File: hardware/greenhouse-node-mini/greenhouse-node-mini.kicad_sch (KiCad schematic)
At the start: 43 parts, among them J1 Molex_KK_396_1x2, J2 JST_XH_2.54mm_1x2, J3 Conn_01x05_Female, J4 Molex_KK_396_1x2, J5 JST_XH_2.54mm_1x4, SW1 SW_Push, U1 ATtiny84A-P, U2 L7805, U3 PCF8574, U4 L298HN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

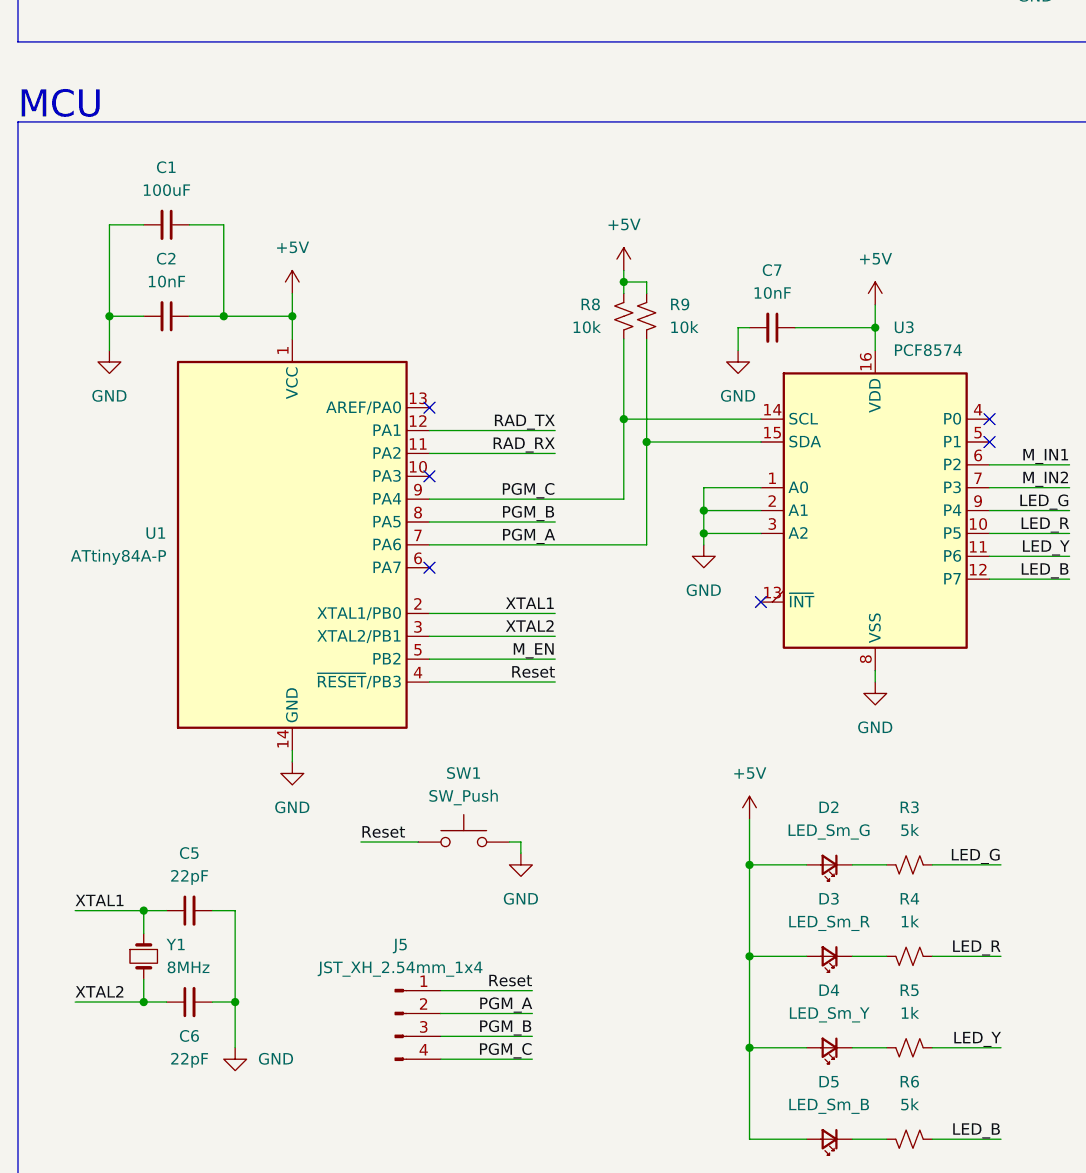
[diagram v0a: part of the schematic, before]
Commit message: Add TODO's for caps
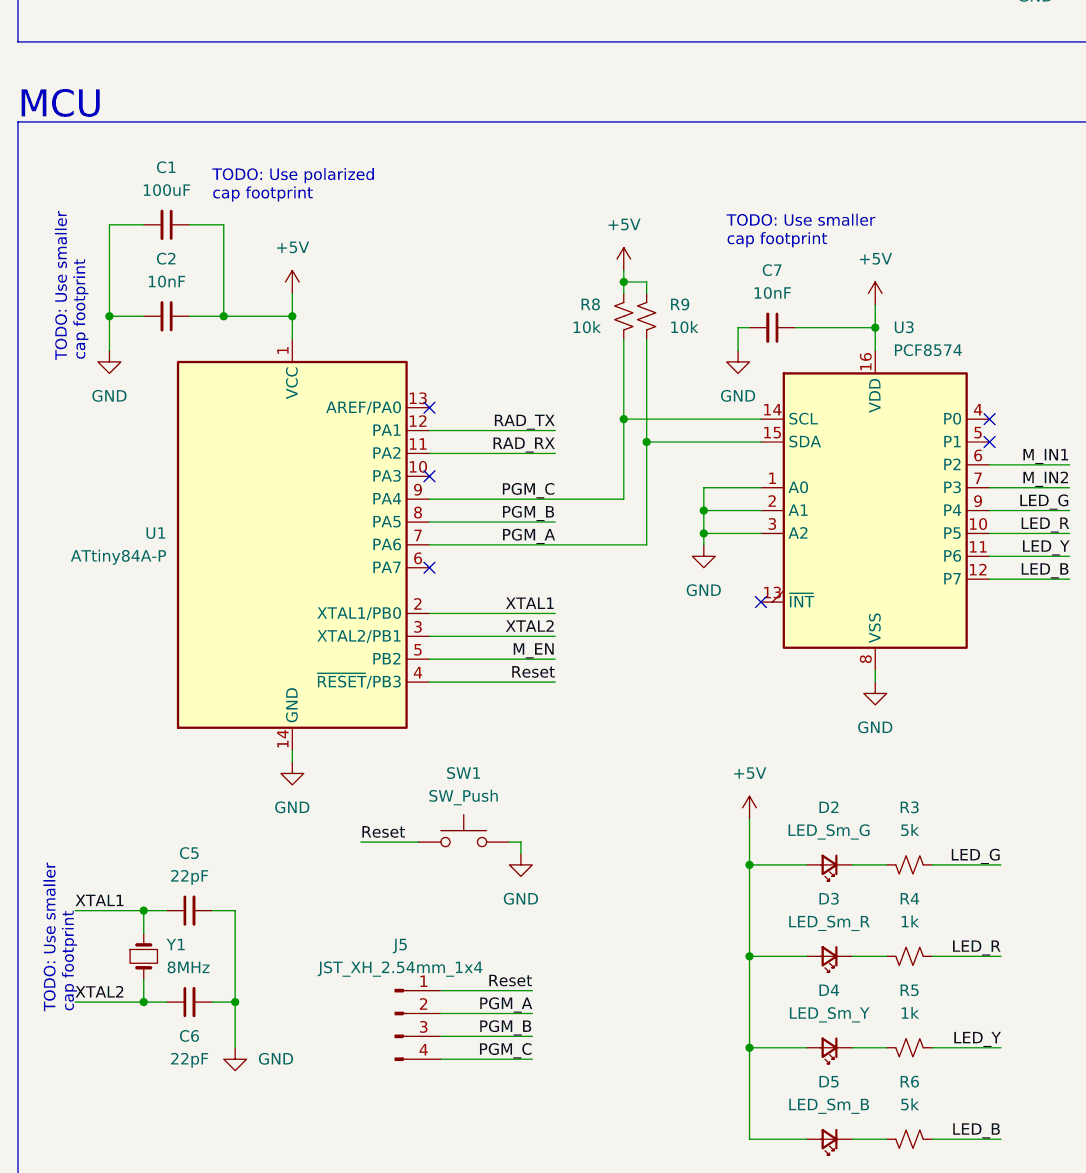
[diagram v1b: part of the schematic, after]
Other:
- note added: "TODO: Use polarized cap footprint"
- note added: "TODO: Use smaller cap footprint"
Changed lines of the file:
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@@
+    (effects (font (size 1.27 1.27)) (justify left bottom))
+  )
+  (text "TODO: Use polarized\ncap footprint" (at 48.26 83.82 0)
+    (effects (font (size 1.27 1.27)) (justify left bottom))
+  )
+  (text "TODO: Use smaller\ncap footprint" (at 105.41 88.9 0)
+    (effects (font (size 1.27 1.27)) (justify left bottom))
+  )
+  (text "TODO: Use smaller\ncap footprint" (at 34.29 101.6 90)
+    (effects (font (size 1.27 1.27)) (justify left bottom))
+  )
+  (text "TODO: Use smaller\ncap footprint" (at 33.02 173.99 90)
     (effects (font (size 1.27 1.27)) (justify left bottom))
   )
